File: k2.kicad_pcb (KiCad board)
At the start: 2 copper layers, 99 x 128.5 mm, 98 parts, among them IC1 TL074, IC2 TL072, IC3 TL074, J1 PJ301_THONKICONN6, J10 PJ301_THONKICONN6, J11 PJ301_THONKICONN6, J12 PJ301_THONKICONN6, J13 Conn_01x05_Female, J14 Conn_01x05_Female, J15 Conn_01x05_Female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

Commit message: v101 to order
tweaks
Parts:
- moved R14 0.20 mm to (156.1, 67.9)
- moved C12 0.20 mm to (144.8, 150.6)
- moved C9 0.20 mm to (157.2, 136.9)
- moved R15 0.11 mm to (151.0, 67.8)
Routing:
- net Net-(IC1-Pad13): track 15.9 -> 15.0 mm
- net InvOutB: track 9.45 -> 10.1 mm
- net VCC: track 133.0 -> 132.5 mm
- net SignInB: track 29.7 -> 29.2 mm
- net GND: vias 57 -> 58
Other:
- board text added: "+ +"
- board text added: "- -"
- board text added: "Crimps V1.0.1 KDS 20211112 karltron.com"
- board text added: "fold caps up"
- board text removed: "Crimps V1.0.1 KDS 20211112"

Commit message: dec2021
status after testing v101
found errors in this board
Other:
- board text added: "Board v101 has errors transistor pinout is upside down input-noise crosstalk triggers trigger. needs re-routing."

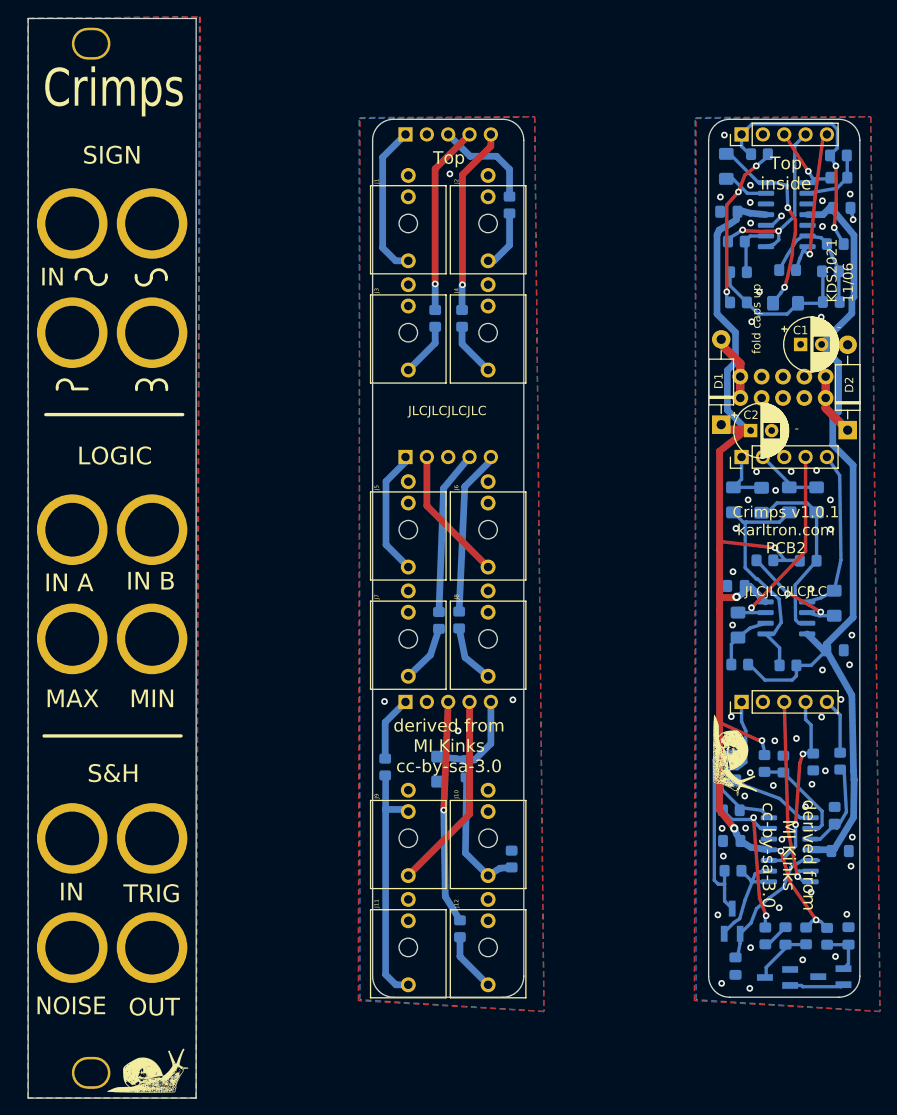
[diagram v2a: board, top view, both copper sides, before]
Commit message: upd to board 1.2
should fix transistor footprint and shift diodes
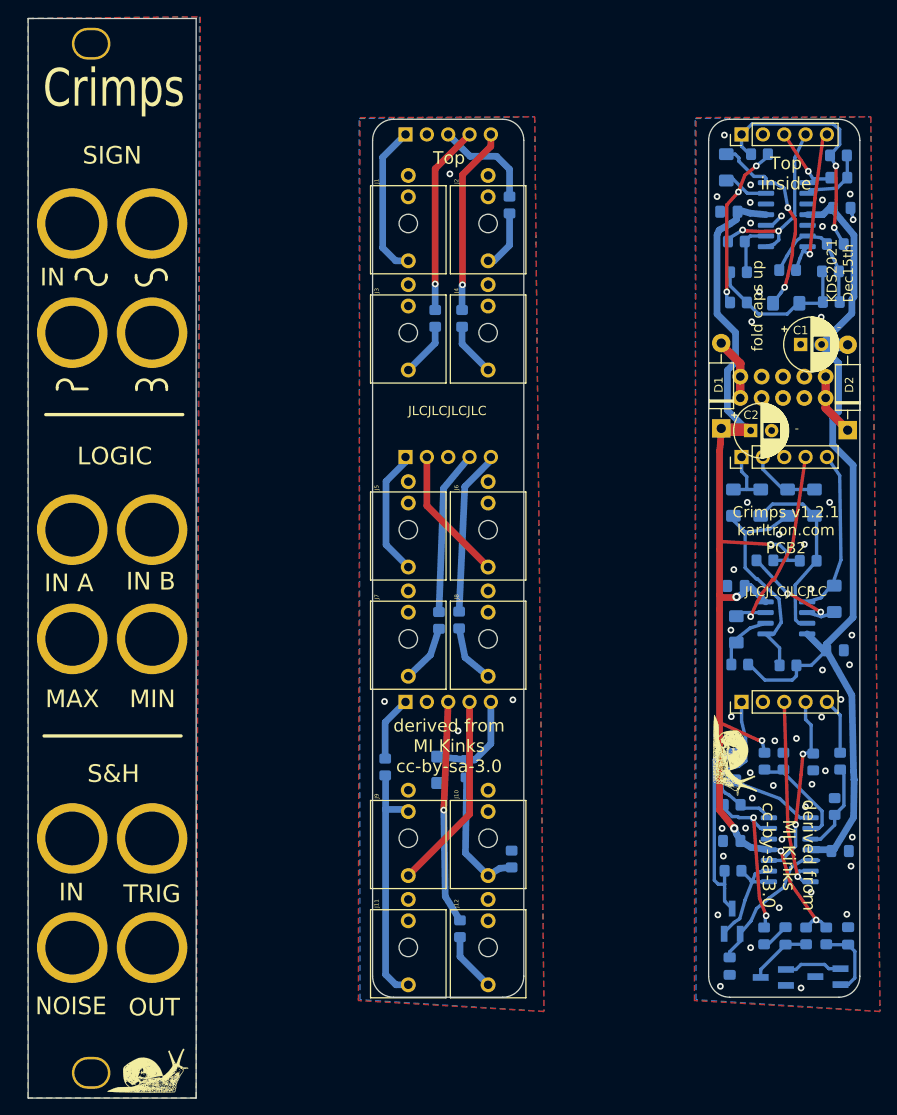
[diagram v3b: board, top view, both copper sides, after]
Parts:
- R27: value 1.5M -> 1M
- moved R28 1.05 mm to (156.6, 131.6)
- moved C12 0.70 mm to (144.1, 150.6)
- moved R27 0.66 mm to (144.4, 131.4)
- moved D11 0.63 mm to (144.9, 110.6)
- moved D10 0.60 mm to (156.6, 106.8)
- moved Q3 0.50 mm to (149.3, 151.9)
- moved D7 0.46 mm to (151.0, 95.5)
- moved D1 0.45 mm to (143.1, 86.6)
- moved D9 0.41 mm to (144.6, 95.5)
- moved D6 0.35 mm to (154.2, 95.3)
- moved Q2 0.35 mm to (155.8, 151.8)
- moved R25 0.35 mm to (150.5, 126.2)
- moved R26 0.27 mm to (148.2, 126.2)
- moved D8 0.22 mm to (147.8, 95.3)
- moved D4 0.20 mm to (143.7, 55.6)
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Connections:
- Q2 pad 1: Net-(C10-Pad1) -> Net-(Q2-Pad1)
- Q2 pad 2: Net-(Q3-Pad2) -> Net-(C10-Pad1)
- Q3 pad 1: GND -> Net-(Q2-Pad1)
- Q3 pad 2: Net-(Q3-Pad2) -> GND
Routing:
- net Net-(Q2-Pad1): track 0.00 -> 6.96 mm
- net Net-(Q3-Pad2): track 6.52 -> 0.00 mm
- net Net-(C10-Pad1): track 5.67 -> 8.88 mm
- net Net-(D7-Pad1): track 29.1 -> 28.4 mm
- net VCC: track 132.5 -> 131.9 mm
- net Net-(C12-Pad1): track 16.8 -> 17.4 mm
- net Net-(IC3-Pad6): track 20.2 -> 20.7 mm
- net GND: vias 58 -> 52
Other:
- board text added: "+"
- board text added: "Crimps v1.2.1 karltron.com PCB2"
- board text added: "KDS2021 Dec15th"
- board text added: "board v 121 is updated for some errors from v101 untested so far, but looks good"
- board text removed: "Board v101 has errors transistor pinout is upside down input-noise crosstalk triggers trigger. needs re-routing."
- board text removed: "Crimps v1.0.1 karltron.com PCB2"

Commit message: versioning
nudge traces
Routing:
- net SHOutB: track 24.7 -> 27.6 mm
- net Net-(C12-Pad1): track 17.4 -> 16.4 mm
- net GND: vias 52 -> 53
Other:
- board text added: "Crimps V1.2.1 KDS 20211112 karltron.com"
- board text added: "Crimps v1.2.1 karltron.com PCB1"
- board text added: "in"
- board text added: "max"
- board text added: "min"
- board text added: "trig"
- board text removed: "Crimps V1.0.1 KDS 20211112 karltron.com"
- board text removed: "Crimps v1.0.1 karltron.com PCB1"

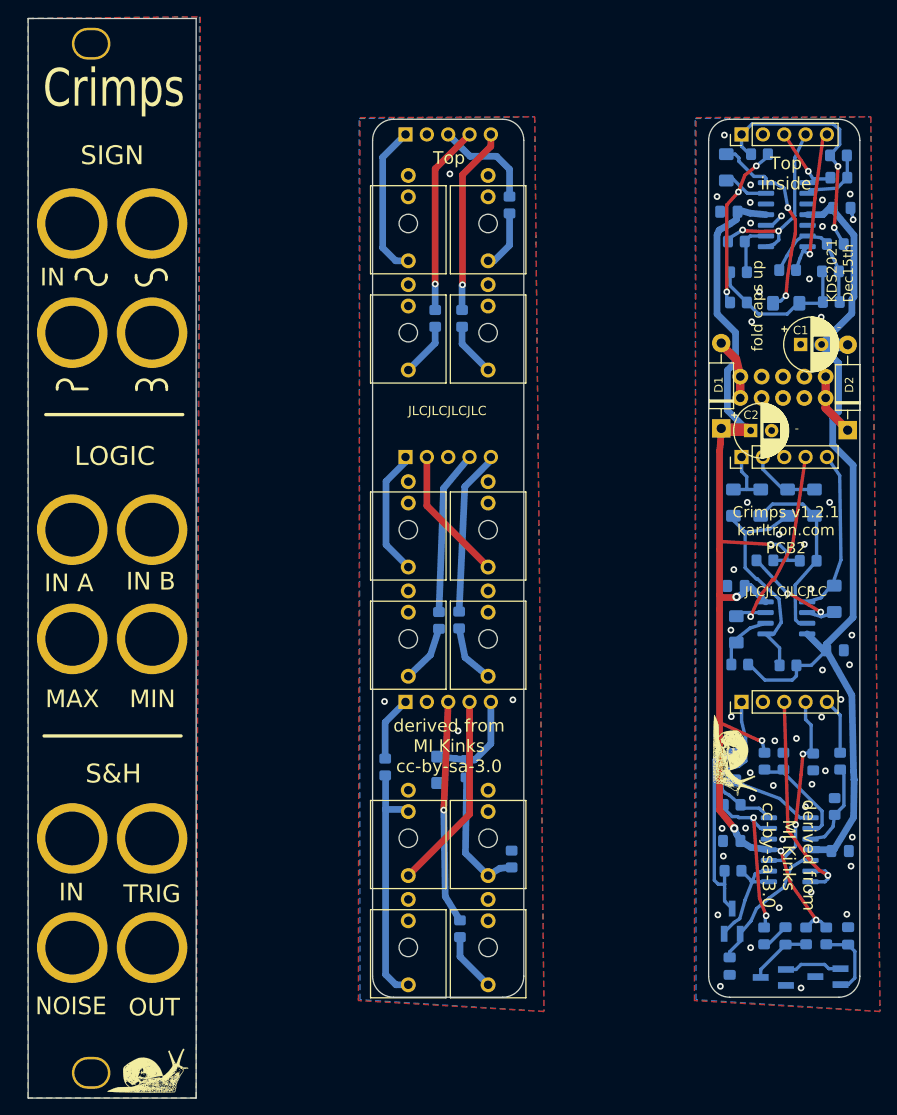
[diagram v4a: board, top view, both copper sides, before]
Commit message: ibom
move files and add an ibom.html
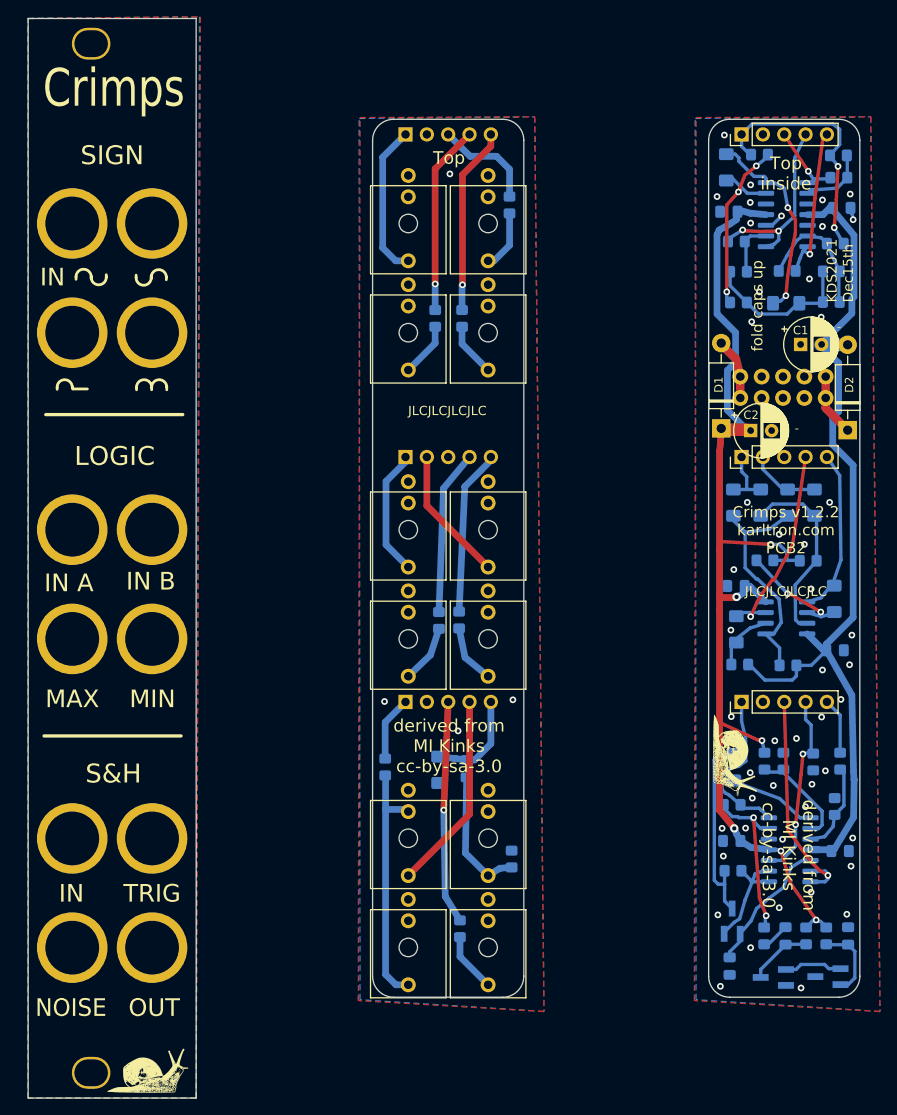
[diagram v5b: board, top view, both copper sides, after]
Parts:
- moved R15 0.11 mm to (150.9, 67.8)
- moved R14 0.10 mm to (156.2, 67.9)
- moved R12 0.05 mm to (156.7, 64.6)
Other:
- board text added: "Crimps V1.2.2 KDS 20211112 karltron.com"
- board text added: "Crimps v1.2.2 karltron.com PCB1"
- board text added: "Crimps v1.2.2 karltron.com PCB2"
- board text removed: "Crimps V1.2.1 KDS 20211112 karltron.com"
- board text removed: "Crimps v1.2.1 karltron.com PCB1"
- board text removed: "Crimps v1.2.1 karltron.com PCB2"
- board text removed: "board v 121 is updated for some errors from v101 untested so far, but looks good"
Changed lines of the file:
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@@
   (general
     (thickness 1.6)
-    (drawings 163)
-    (tracks 522)
+    (drawings 162)
+    (tracks 521)
     (zones 0)
     (modules 98)
@@
     (title Crimps)
     (date 2021-12-15)
-    (rev 1.2.1)
+    (rev 1.2.2)
     (company karltron.com)
     (comment 1 "Kinks Clone")
@@
   )
   (setup
-    (last_trace_width 0.4)
+    (last_trace_width 0.25)
     (user_trace_width 0.4)
     (user_trace_width 0.8)
@@
     (tags "diode handsolder")
     (attr smd)
-    (fp_text reference D11 (at -0.2 -2.2 90) (layer B.SilkS)
+    (fp_text reference D11 (at -0.15 -2.1 90) (layer B.SilkS)
       (effects (font (size 1 1) (thickness 0.15)) (justify mirror))
     )
@@
   )
   (module Resistor_SMD:R_0805_2012Metric_Pad1.20x1.40mm_HandSolder (layer B.Cu)
-    (at 147.65 53.95 180)
+    (at 147.65 54 180)
     (descr "Resistor SMD 0805 (2012 Metric), square (rectangular) end terminal, IPC_7351 nominal with elongated pad for handsoldering. (Body size source: IPC-SM-782 page 72, https://www.pcb-3d.com/wordpress/wp-content/uploads/ipc-sm-782a_amendment_1_and_2.pdf), generated with kicad-footprint-generator")
     (tags "resistor handsolder")
@@
     (tags SOT-23)
     (attr smd)
-    (fp_text reference Q1 (at 1.1 -1.1 270) (layer B.SilkS)
+    (fp_text reference Q1 (at 0.95 -1.1 270) (layer B.SilkS)
       (effects (font (size 1 1) (thickness 0.15)) (justify right bottom mirror))
     )
@@
     (tags "capacitor handsolder")
     (attr smd)
-    (fp_text reference C7 (at 0 -2) (layer B.SilkS)
+    (fp_text reference C7 (at -0.05 -1.9) (layer B.SilkS)
       (effects (font (size 1 1) (thickness 0.15)) (justify mirror))
     )
@@
     (tags "capacitor handsolder")
     (attr smd)
-    (fp_text reference C12 (at 0 1.5 270) (layer B.SilkS)
+    (fp_text reference C12 (at 0 1.55 270) (layer B.SilkS)
       (effects (font (size 1 1) (thickness 0.15)) (justify mirror))
     )
@@
   )
   (module Resistor_SMD:R_0805_2012Metric_Pad1.20x1.40mm_HandSolder (layer B.Cu)
-    (at 145.15 68 180)
+    (at 145.15 67.95 180)
     (descr "Resistor SMD 0805 (2012 Metric), square (rectangular) end terminal, IPC_7351 nominal with elongated pad for handsoldering. (Body size source: IPC-SM-782 page 72, https://www.pcb-3d.com/wordpress/wp-content/uploads/ipc-sm-782a_amendment_1_and_2.pdf), generated with kicad-footprint-generator")
     (tags "resistor handsolder")
@@
   )
   (module Resistor_SMD:R_0805_2012Metric_Pad1.20x1.40mm_HandSolder (layer B.Cu)
-    (at 151 67.75 180)
+    (at 150.95 67.85 180)
     (descr "Resistor SMD 0805 (2012 Metric), square (rectangular) end terminal, IPC_7351 nominal with elongated pad for handsoldering. (Body size source: IPC-SM-782 page 72, https://www.pcb-3d.com/wordpress/wp-content/uploads/ipc-sm-782a_amendment_1_and_2.pdf), generated with kicad-footprint-generator")
     (tags "resistor handsolder")
@@
   )
   (module Resistor_SMD:R_0805_2012Metric_Pad1.20x1.40mm_HandSolder (layer B.Cu)
-    (at 156.1 67.9 180)
+    (at 156.2 67.9 180)
     (descr "Resistor SMD 0805 (2012 Metric), square (rectangular) end terminal, IPC_7351 nominal with elongated pad for handsoldering. (Body size source: IPC-SM-782 page 72, https://www.pcb-3d.com/wordpress/wp-content/uploads/ipc-sm-782a_amendment_1_and_2.pdf), generated with kicad-footprint-generator")
     (tags "resistor handsolder")
@@
   )
   (module Resistor_SMD:R_0805_2012Metric_Pad1.20x1.40mm_HandSolder (layer B.Cu)
-    (at 156.675 64.65)
+    (at 156.675 64.6)
     (descr "Resistor SMD 0805 (2012 Metric), square (rectangular) end terminal, IPC_7351 nominal with elongated pad for handsoldering. (Body size source: IPC-SM-782 page 72, https://www.pcb-3d.com/wordpress/wp-content/uploads/ipc-sm-782a_amendment_1_and_2.pdf), generated with kicad-footprint-generator")
     (tags "resistor handsolder")
@@
     (tags "resistor handsolder")
     (attr smd)
-    (fp_text reference R22 (at 0 1.65) (layer B.SilkS)
+    (fp_text reference R22 (at 0 1.7) (layer B.SilkS)
       (effects (font (size 1 1) (thickness 0.15)) (justify mirror))
     )
@@
     (tags "resistor handsolder")
     (attr smd)
-    (fp_text reference R21 (at 0 1.65) (layer B.SilkS)
+    (fp_text reference R21 (at -0.05 1.7) (layer B.SilkS)
       (effects (font (size 1 1) (thickness 0.15)) (justify mirror))
     )
@@
     (tags "resistor handsolder")
     (attr smd)
-    (fp_text reference R25 (at -3.85 -0.1 90) (layer B.SilkS)
+    (fp_text reference R25 (at -3.75 -0.1 90) (layer B.SilkS)
       (effects (font (size 1 1) (thickness 0.15)) (justify mirror))
     )
@@
     (tags "resistor handsolder")
     (attr smd)
-    (fp_text reference R27 (at -0.1 -1.85) (layer B.SilkS)
+    (fp_text reference R27 (at -0.05 -1.75) (layer B.SilkS)
       (effects (font (size 1 1) (thickness 0.15)) (justify mirror))
     )
@@
     (tags "resistor handsolder")
     (attr smd)
-    (fp_text reference R23 (at -3.65 -0.1 90) (layer B.SilkS)
+    (fp_text reference R23 (at -3.6 -0.1 90) (layer B.SilkS)
       (effects (font (size 1 1) (thickness 0.15)) (justify mirror))
     )
@@
     (tags "resistor handsolder")
     (attr smd)
-    (fp_text reference R29 (at -0.1 1.9) (layer B.SilkS)
+    (fp_text reference R29 (at 0 1.8) (layer B.SilkS)
       (effects (font (size 1 1) (thickness 0.15)) (justify mirror))
     )
@@
       (net 1 GND))
   )
-  (gr_text in (at 153.25 117.4 -90) (layer B.SilkS)
+  (gr_text in (at 153.25 117.35 -90) (layer B.SilkS)
     (effects (font (size 1 1) (thickness 0.2)) (justify mirror))
   )
@@
     (effects (font (size 2 2) (thickness 0.5)) (justify mirror))
   )
-  (gr_text "board v 121 is updated for some errors from v101\nuntested so far, but looks good" (at 201.6 131.4) (layer Cmts.User)
-    (effects (font (size 2 2) (thickness 0.15)))
-  )
   (gr_text . (at 150.45 139.8) (layer B.SilkS)
     (effects (font (size 2 2) (thickness 0.5)) (justify mirror))
   )
-  (gr_text "Crimps v1.2.1\nkarltron.com\nPCB1" (at 110.5 84.55) (layer B.SilkS)
+  (gr_text "Crimps v1.2.2\nkarltron.com\nPCB1" (at 110.5 84.55) (layer B.SilkS)
     (effects (font (size 1.33 1.33) (thickness 0.25)) (justify mirror))
   )
@@
     (effects (font (size 1 1) (thickness 0.2)) (justify mirror))
   )
-  (gr_text S (at 146.6 146.6) (layer B.SilkS)
+  (gr_text S (at 146.55 146.65) (layer B.SilkS)
     (effects (font (size 1 1) (thickness 0.2)) (justify mirror))
   )
-  (gr_text D (at 142.3 146.7 180) (layer B.SilkS)
+  (gr_text D (at 142.35 146.75 180) (layer B.SilkS)
     (effects (font (size 1 1) (thickness 0.2)))
   )
@@
     (effects (font (size 2 2) (thickness 0.5)) (justify mirror))
   )
-  (gr_text "Crimps v1.2.1\nkarltron.com\nPCB2" (at 150.8 98.7) (layer F.SilkS)
+  (gr_text "Crimps v1.2.2\nkarltron.com\nPCB2" (at 150.8 98.7) (layer F.SilkS)
     (effects (font (size 1.33 1.33) (thickness 0.25)))
   )
@@
     (effects (font (size 2.25 2.25) (thickness 0.4)))
   )
-  (gr_text TRIG (at 75.35 142) (layer F.SilkS)
+  (gr_text TRIG (at 75.35 141.95) (layer F.SilkS)
     (effects (font (size 2.1 2.1) (thickness 0.4)))
   )
-  (gr_text NOISE (at 65.7 155.35) (layer F.SilkS)
+  (gr_text NOISE (at 65.7 155.55) (layer F.SilkS)
     (effects (font (size 2.1 2) (thickness 0.4)))
   )
-  (gr_text IN (at 65.75 141.8) (layer F.SilkS)
+  (gr_text IN (at 65.75 141.95) (layer F.SilkS)
     (effects (font (size 2.1 2.1) (thickness 0.4)))
   )
-  (gr_text OUT (at 75.6 155.5) (layer F.SilkS)
+  (gr_text OUT (at 75.6 155.55) (layer F.SilkS)
     (effects (font (size 2.1 2.1) (thickness 0.4)))
   )
@@
   )
   (gr_line (start 80.9 57.5) (end 80.9 49.4) (layer Dwgs.User) (width 0.15))
-  (gr_text "Crimps V1.2.1\nKDS 20211112\nkarltron.com" (at 70.95 48.45) (layer B.SilkS)
+  (gr_text "Crimps V1.2.2\nKDS 20211112\nkarltron.com" (at 70.95 48.45) (layer B.SilkS)
     (effects (font (size 1.5 1.5) (thickness 0.3)) (justify mirror))
   )
@@
   (gr_line (start 54.1 58.3) (end 54.1 124) (layer F.Fab) (width 0.15))
   (via (at 143 153) (size 0.8) (drill 0.4) (layers F.Cu B.Cu) (net 1))
-  (via (at 158.7 135.25) (size 0.8) (drill 0.4) (layers F.Cu B.Cu) (net 1))
   (via (at 150 143.65) (size 0.8) (drill 0.4) (layers F.Cu B.Cu) (net 1))
   (via (at 153.8 141.8) (size 0.8) (drill 0.4) (layers F.Cu B.Cu) (net 1))
@@
   (via (at 150.4 135.5) (size 0.8) (drill 0.4) (layers F.Cu B.Cu) (net 1))
   (via (at 153.6 68.8) (size 0.8) (drill 0.4) (layers F.Cu B.Cu) (net 1))
+  (via (at 158.75 135.35) (size 0.8) (drill 0.4) (layers F.Cu B.Cu) (net 1))
   (segment (start 156.55 136.7) (end 158.85 132.9) (width 0.8) (layer B.Cu) (net 2) (status 10))
   (segment (start 158.921585 128.421585) (end 158.9 128.4) (width 0.8) (layer B.Cu) (net 2))
@@
   (segment (start 155.05 71.7) (end 155.2 71.55) (width 0.4) (layer B.Cu) (net 23) (status 30))
   (segment (start 155.2 71.55) (end 155.2 67.8) (width 0.4) (layer B.Cu) (net 23) (status 30))
-  (segment (start 155.2 67.8) (end 155.1 67.7) (width 0.4) (layer B.Cu) (net 23) (status 30))
   (via (at 151 106.275) (size 0.8) (drill 0.4) (layers F.Cu B.Cu) (net 24))
   (segment (start 151 106.275) (end 147.65 102.65) (width 0.4) (layer B.Cu) (net 24) (status 20))

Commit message: logo added
adding WEEE wheelie bin
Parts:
- added REF**: WEEE-Logo_5.6x8mm_SilkScreen, Symbol:WEEE-Logo_5.6x8mm_SilkScreen, B.Cu at (75.5, 41.2)
- added REF**: WEEE-Logo_5.6x8mm_SilkScreen, Symbol:WEEE-Logo_5.6x8mm_SilkScreen, F.Cu at (150.8, 60.8)
